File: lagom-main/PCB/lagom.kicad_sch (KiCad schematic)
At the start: 168 parts, among them J1 Conn_01x04, J2 Conn_01x03, SW83 RotaryEncoder_Switch, SW84 RotaryEncoder_Switch, U1 ProMicro, U2 74HC138, U3 74HC138

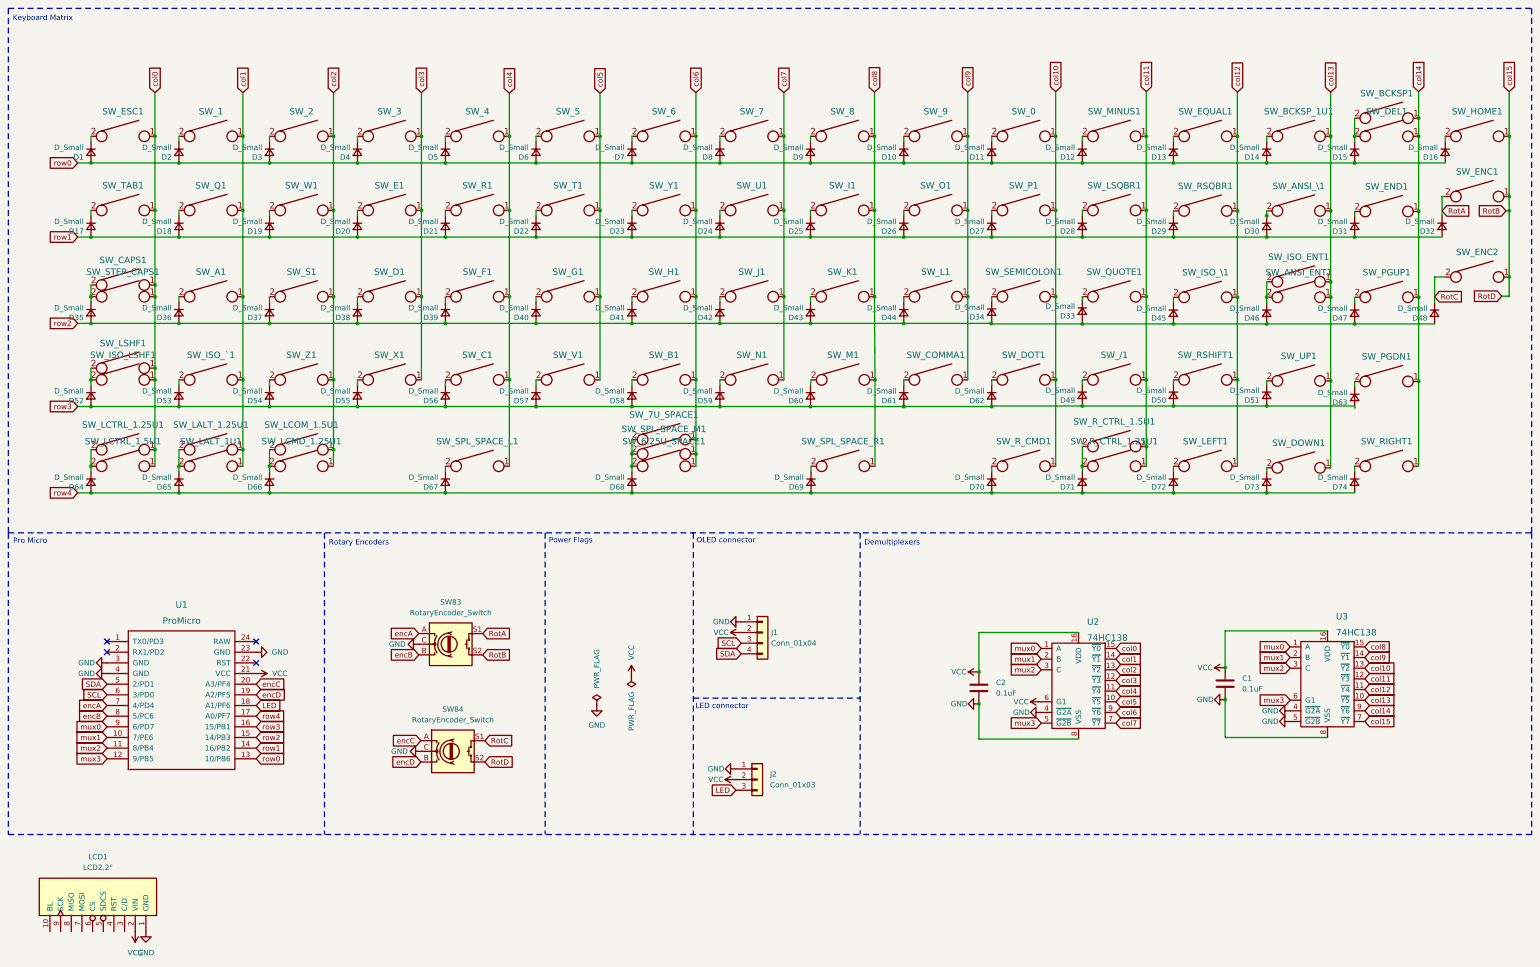
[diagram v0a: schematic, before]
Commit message: Changed PCB To Use a RPI Pico and Fixed Wiring Routes
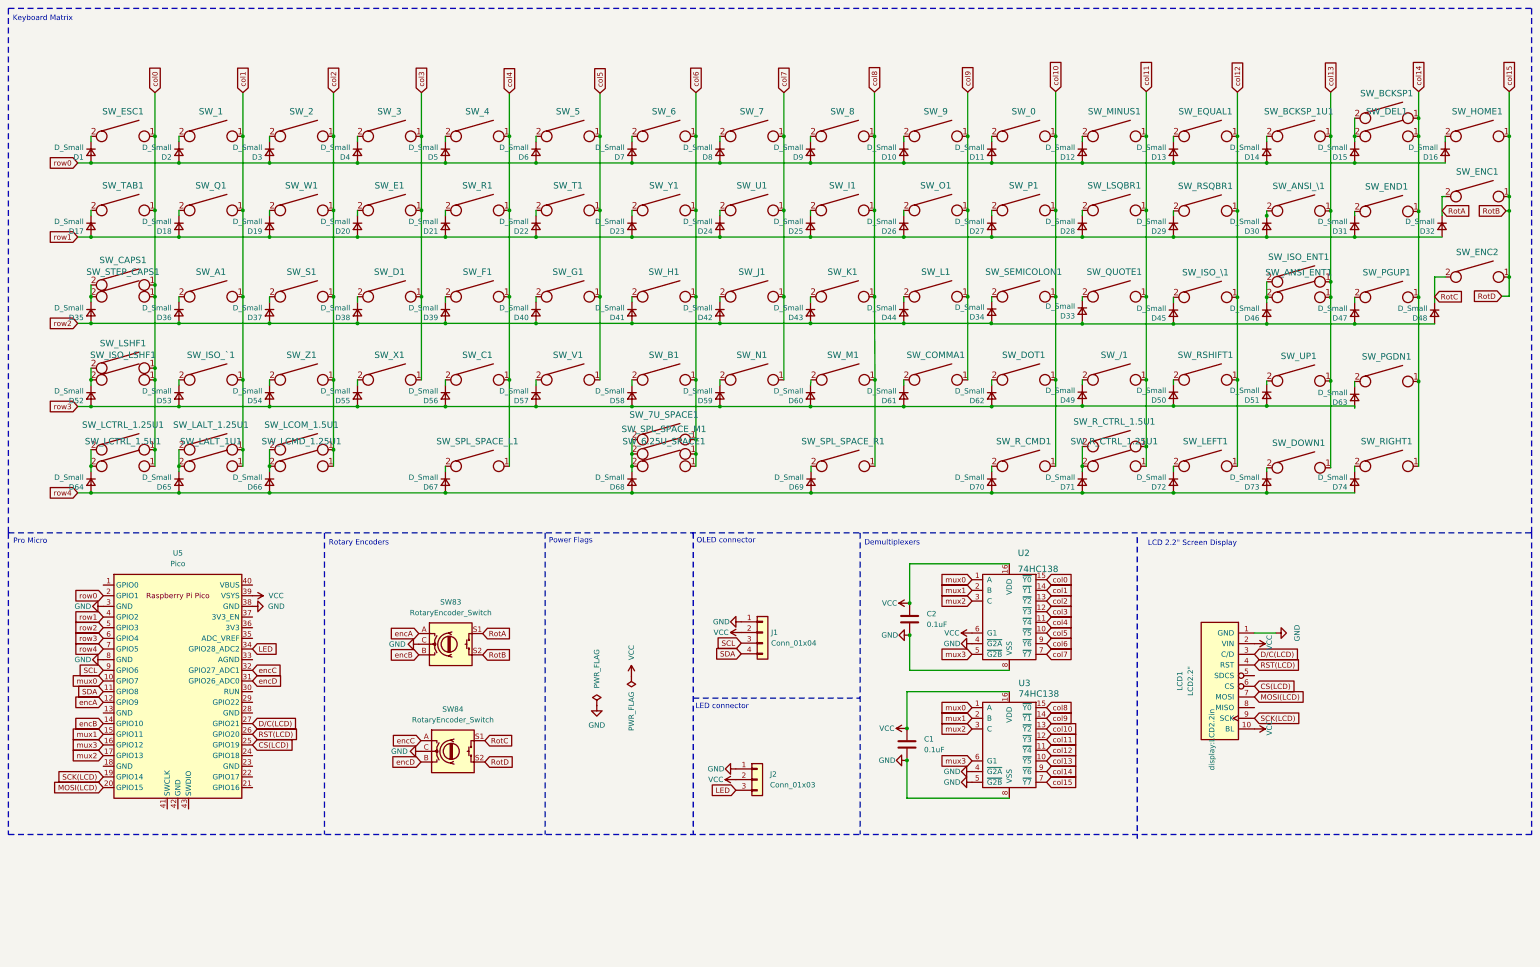
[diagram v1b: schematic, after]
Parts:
- removed U1: ProMicro, Keebio-Parts:ArduinoProMicro-ZigZag, symbol keebio:ProMicro
- added U5: Pico, MCU_RaspberryPi_and_Boards:RPi_Pico_SMD_TH, symbol MCU_RaspberryPi_and_Boards:Pico
- LCD1: footprint (none) -> display:LCD2.2in
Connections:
- net GND: now also U5.3 (GND), U5.38 (GND), U5.8 (GND)
- net LED: now also U5.34 (GPIO28_ADC2)
- net SCL: now also U5.9 (GPIO6)
- net SDA: now also U5.11 (GPIO8)
- net VCC: now also LCD1.10 (BL), U5.39 (VSYS)
- net encA: now also U5.12 (GPIO9)
- net encB: now also U5.14 (GPIO10)
- net encC: now also U5.32 (GPIO27_ADC1)
- net encD: now also U5.31 (GPIO26_ADC0)
- net mux0: now also U5.10 (GPIO7)
- net mux1: now also U5.15 (GPIO11)
- net mux2: now also U5.17 (GPIO13)
- net mux3: now also U5.16 (GPIO12)
- net row0: now also U5.2 (GPIO1)
- net row1: now also U5.4 (GPIO2)
- net row2: now also U5.5 (GPIO3)
- net row3: now also U5.6 (GPIO4)
- net row4: now also U5.7 (GPIO5)
- net D/C(LCD): now reaches LCD1.3 (C/D)
- net D/C(LCD): now also U5.27 (GPIO21)
- net RST(LCD): now reaches LCD1.4 (RST)
- net RST(LCD): now also U5.26 (GPIO20)
- net CS(LCD): now reaches LCD1.6 (CS)
- net CS(LCD): now also U5.25 (GPIO19)
- net MOSI(LCD): now reaches LCD1.7 (MOSI)
- net MOSI(LCD): now also U5.20 (GPIO15)
- net SCK(LCD): now reaches LCD1.9 (SCK)
- net SCK(LCD): now also U5.19 (GPIO14)
- no-connect marks 4 -> 0
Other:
- note added: "LCD 2.2" Screen Display"
- moved on the sheet: C1, C2, LCD1, U2, U3
